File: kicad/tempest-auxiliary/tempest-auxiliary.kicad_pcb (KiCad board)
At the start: 2 copper layers, 188 x 180 mm, 23 parts

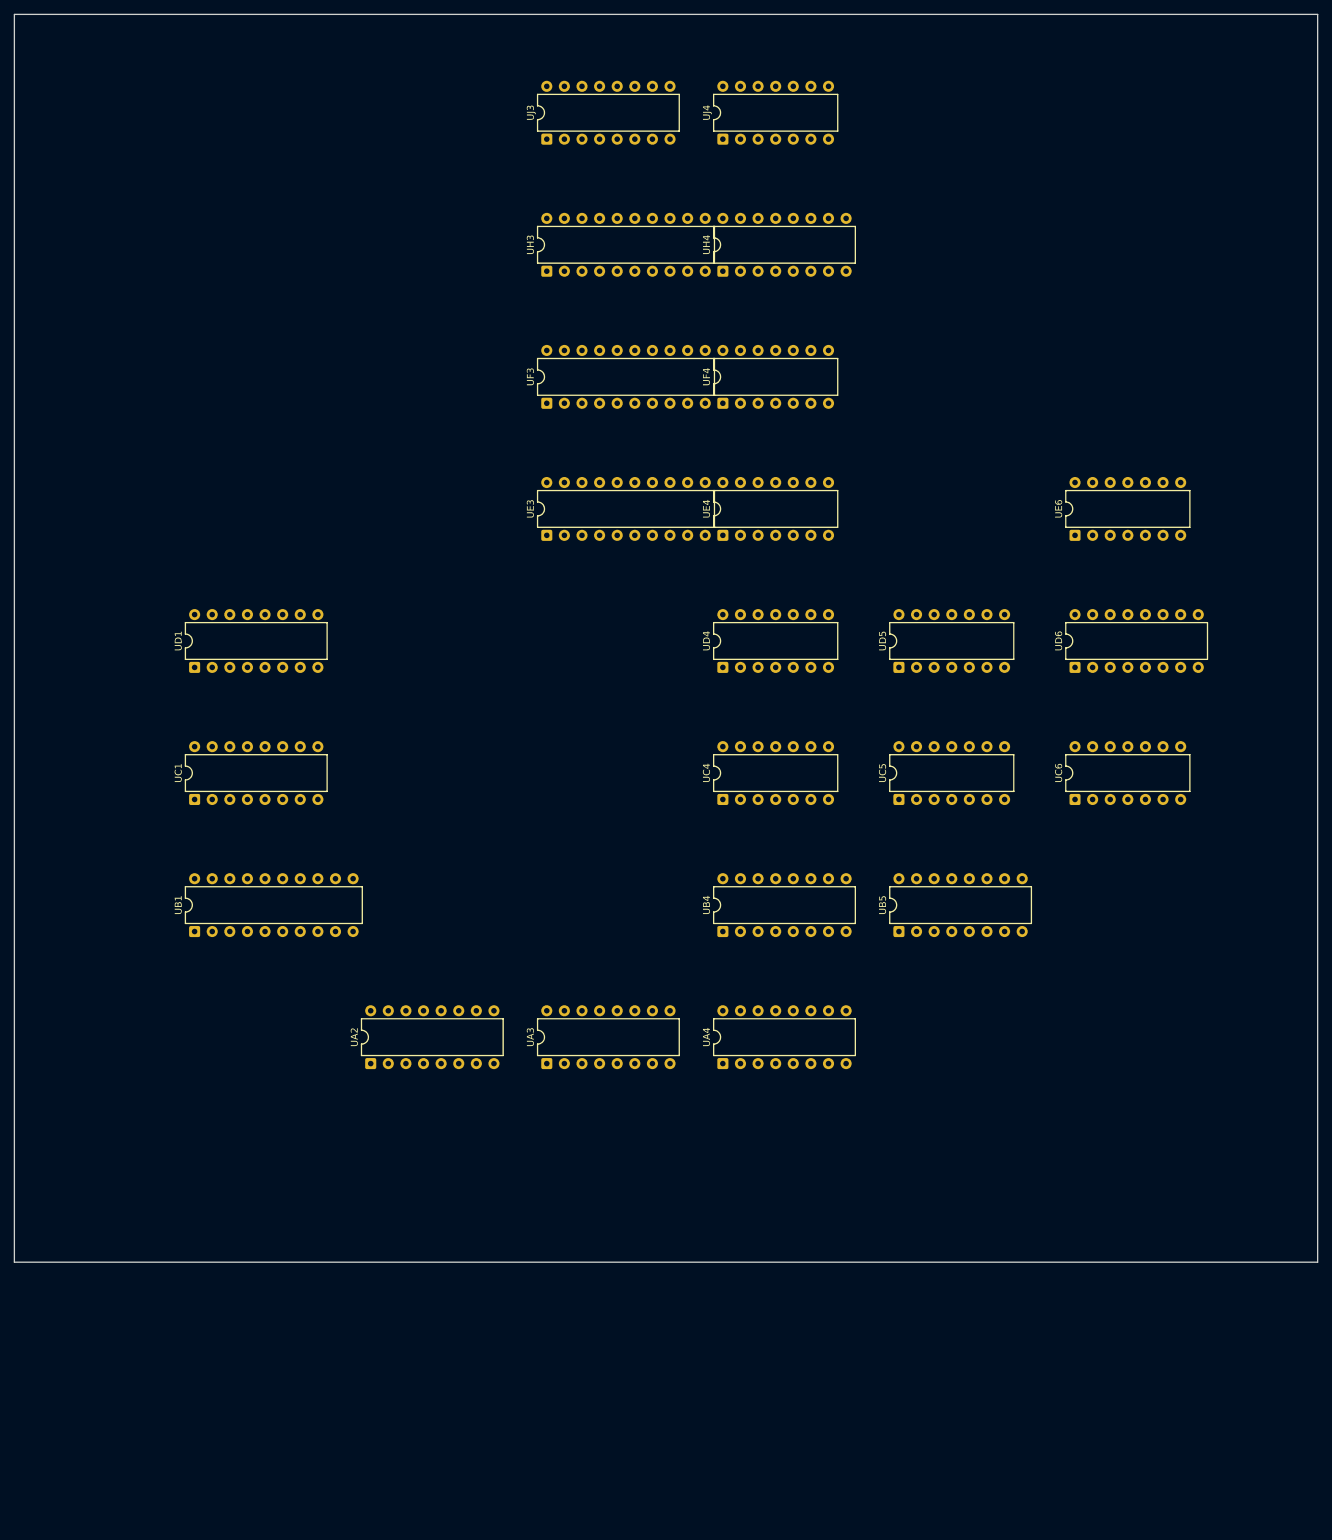
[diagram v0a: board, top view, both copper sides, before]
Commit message: Trace the Tempest Auxiliary PCB in full and redraw it in KiCad
Every connection on DP-190 sheet 3 Side B (Auxiliary PCB 037585-01, 4th
printing, checked against the 2nd and 1st) read into
boards/tempest-auxiliary.nets: 216 nets over 1,036 pins, 41 ICs and 147
passives, connectors and test points. It is not "23 stock parts": the sheet
carries the whole Math Box, the ER2055 high-score EAROM and the charge pump
that makes its -28V, both POKEYs, the spinner inputs and the audio stage.

Checks, all passing:
- build_board_nets.py: 0 problems.
- Every one of the 130 resistor, capacitor and diode values, and all 41 IC
  positions, agree with the TM-190 Figure 22 parts list.
- The Math Box, mapped onto Battlezone's positions, agrees with the
  independently traced Battlezone board on all 79 nets and all 65 signatures.
- check_board_schematic.py: KiCad's netlist of the eleven redrawn sheets
  matches the read, 0 disagreements.

The pipeline is now generic:
- plan_board_schematic.py takes its layout from boards/<slug>.sheets.json
  (Battlezone's plan regenerates byte for byte) and, with --ops, writes every
  label, power symbol and no-connect at an explicit coordinate from the
  symbol geometry -- the way round Konnect's first-unit-only pin queries.
- tools/check_board_sheets.py proves one sheet as soon as it is drawn.
- build_board_nets.py: `parallel` for outputs tied on purpose (K3's four
  LM324 sections), a custom pinout may name a supply pin's rail (the ER2055's
  VSS is +5V), any +/-NV net is a rail, and a net with two sheet names takes
  the first declared rather than whichever hash order picked.
- docs/TRACING-A-BOARD.md is the reader brief and the drawing recipe.

Logged, not guessed: B1 pin 1 is lettered BEGIN but drawn wired to /BEGIN in
all three printings (the read follows the label); K3, R58, C39, three
signatures and R10's supply differ between printings. The site does not
render board notes or conflicts, so the BEGIN one is in the status line too.

ERC has 5 er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
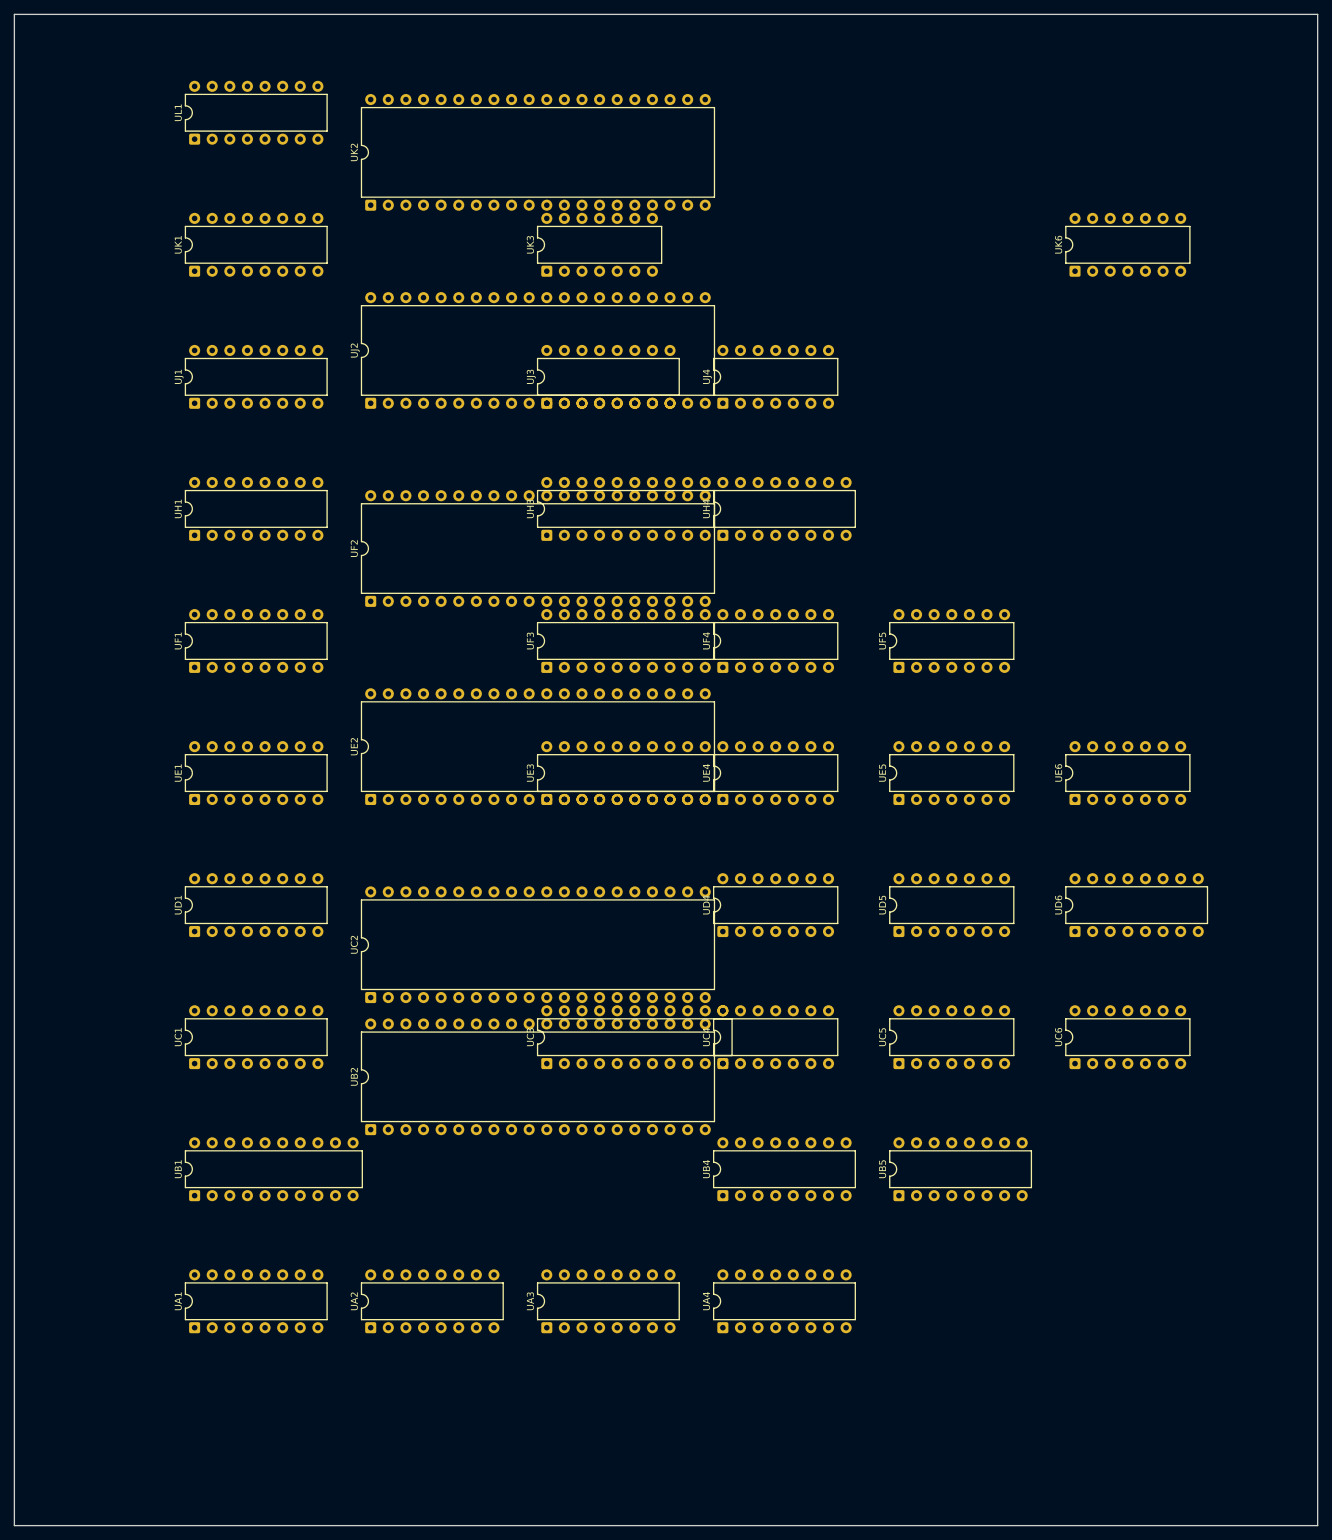
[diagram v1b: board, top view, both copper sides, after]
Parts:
- added UA1: 82S123, DIP-16_W7.62mm, F.Cu at (26.0, 189.4)
- added UB2: C012294-01, DIP-40_W15.24mm, F.Cu at (51.4, 160.9)
- added UC2: C012294-01, DIP-40_W15.24mm, F.Cu at (51.4, 141.8)
- added UC3: ER2055, DIP-22_W7.62mm, F.Cu at (76.8, 151.3)
- added UE1: 82S129, DIP-16_W7.62mm, F.Cu at (26.0, 113.2)
- added UE2: 137004-001, DIP-40_W15.24mm, F.Cu at (51.4, 113.2)
- added UE5: 74S86, DIP-14_W7.62mm, F.Cu at (127.6, 113.2)
- added UF1: 82S129, DIP-16_W7.62mm, F.Cu at (26.0, 94.2)
- added UF2: 137004-001, DIP-40_W15.24mm, F.Cu at (51.4, 84.7)
- added UF5: 74S03, DIP-14_W7.62mm, F.Cu at (127.6, 94.2)
- added UH1: 82S129, DIP-16_W7.62mm, F.Cu at (26.0, 75.2)
- added UJ1: 82S129, DIP-16_W7.62mm, F.Cu at (26.0, 56.1)
- added UJ2: 137004-001, DIP-40_W15.24mm, F.Cu at (51.4, 56.1)
- added UK1: 82S129, DIP-16_W7.62mm, F.Cu at (26.0, 37.0)
- added UK2: 137004-001, DIP-40_W15.24mm, F.Cu at (51.4, 27.5)
- added UK3: LM324, DIP-14_W7.62mm, F.Cu at (76.8, 37.0)
- added UK6: LM324, DIP-14_W7.62mm, F.Cu at (153.0, 37.0)
- added UL1: 82S129, DIP-16_W7.62mm, F.Cu at (26.0, 18.0)
- moved UD1 38.1 mm to (26.0, 132.3)
- moved UD4 38.1 mm to (102.2, 132.3)
- moved UD5 38.1 mm to (127.6, 132.3)
- moved UD6 38.1 mm to (153.0, 132.3)
- moved UH3 38.1 mm to (76.8, 75.2)
- moved UH4 38.1 mm to (102.2, 75.2)
- moved UF3 38.1 mm to (76.8, 94.2)
- moved UF4 38.1 mm to (102.2, 94.2)
- moved UJ3 38.1 mm to (76.8, 56.1)
- moved UJ4 38.1 mm to (102.2, 56.1)
- moved UA2 38.1 mm to (51.4, 189.4)
- moved UA3 38.1 mm to (76.8, 189.4)
- moved UA4 38.1 mm to (102.2, 189.4)
- moved UB1 38.1 mm to (26.0, 170.4)
- moved UB4 38.1 mm to (102.2, 170.4)
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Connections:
- UA2 pad 1: (no net) -> M START
- UA2 pad 16: (no net) -> +5V
- UA2 pad 2: (no net) -> E3MHZ
- UA2 pad 3: (no net) -> /BEGIN
- UA2 pad 4: (no net) -> E6MHZ
- UA2 pad 5: (no net) -> R1-1
- UA2 pad 6: (no net) -> BEGIN
- UA2 pad 7: (no net) -> /BEGIN
- UA2 pad 8: (no net) -> GND
- UA3 pad 1: (no net) -> R1-1
- UA3 pad 10: (no net) -> A3-10
- UA3 pad 11: (no net) -> EAB1
- UA3 pad 12: (no net) -> A3-12
- UA3 pad 13: (no net) -> EAB3
- UA3 pad 14: (no net) -> EAB5
- UA3 pad 15: (no net) -> A3-15
- UA3 pad 16: (no net) -> +5V
- UA3 pad 2: (no net) -> A3-2
- UA3 pad 3: (no net) -> EAB4
- UA3 pad 4: (no net) -> EAB2
- UA3 pad 5: (no net) -> A3-5
- UA3 pad 6: (no net) -> EAB0
- UA3 pad 7: (no net) -> A3-7
- UA3 pad 8: (no net) -> GND
- UA3 pad 9: (no net) -> /EARWR
- UA4 pad 1: (no net) -> GND
- UA4 pad 10: (no net) -> GND
- UA4 pad 11: (no net) -> R54-1
- UA4 pad 14: (no net) -> D6-12
- UA4 pad 15: (no net) -> GND
- UA4 pad 16: (no net) -> +5V
- UA4 pad 2: (no net) -> TBC1
- UA4 pad 3: (no net) -> TBC0
- UA4 pad 4: (no net) -> GND
- UA4 pad 5: (no net) -> C6-5
- UA4 pad 6: (no net) -> TBC2
- UA4 pad 7: (no net) -> TBC3
- UA4 pad 8: (no net) -> GND
- UA4 pad 9: (no net) -> GND
- UB1 pad 1: (no net) -> BEGIN
- UB1 pad 10: (no net) -> GND
- UB1 pad 11: (no net) -> E4-6
- UB1 pad 12: (no net) -> A1-7
- UB1 pad 13: (no net) -> A1
- UB1 pad 14: (no net) -> A3
- UB1 pad 15: (no net) -> A1-5
- UB1 pad 16: (no net) -> A1-3
- UB1 pad 17: (no net) -> A5
- UB1 pad 18: (no net) -> A7
- UB1 pad 19: (no net) -> A1-1
- UB1 pad 2: (no net) -> A1-2
- UB1 pad 20: (no net) -> +5V
- UB1 pad 3: (no net) -> A6
- UB1 pad 4: (no net) -> A4
- UB1 pad 5: (no net) -> A1-4
- UB1 pad 6: (no net) -> A1-6
- UB1 pad 7: (no net) -> A2
- UB1 pad 8: (no net) -> A0
- UB1 pad 9: (no net) -> A1-9
- UB4 pad 1: (no net) -> /I/O
- UB4 pad 11: (no net) -> /EARCON
- UB4 pad 12: (no net) -> /EARWR
- UB4 pad 13: (no net) -> EAB7
- UB4 pad 14: (no net) -> EAB6
- UB4 pad 15: (no net) -> C4-3
- UB4 pad 16: (no net) -> +5V
- UB4 pad 2: (no net) -> EAB6
- UB4 pad 3: (no net) -> EAB7
- UB4 pad 5: (no net) -> B4-5
- UB4 pad 6: (no net) -> B4-6
- UB4 pad 7: (no net) -> B4-7
- UB4 pad 8: (no net) -> GND
- UB5 pad 1: (no net) -> B4-7
- UB5 pad 10: (no net) -> /YLO
- UB5 pad 11: (no net) -> /EARD
- UB5 pad 12: (no net) -> /STREN
- UB5 pad 13: (no net) -> EAB5
- UB5 pad 14: (no net) -> EAB4
- UB5 pad 15: (no net) -> C4-8
- UB5 pad 16: (no net) -> +5V
- UB5 pad 2: (no net) -> EAB4
- UB5 pad 3: (no net) -> EAB5
- UB5 pad 4: (no net) -> /POKEY1
- UB5 pad 5: (no net) -> /POKEY2
- UB5 pad 6: (no net) -> B5-6
- UB5 pad 8: (no net) -> GND
- UB5 pad 9: (no net) -> /YHI
- UC1 pad 1: (no net) -> R1-1
- UC1 pad 10: (no net) -> /PCEN
- UC1 pad 11: (no net) -> SAEN1
- UC1 pad 12: (no net) -> MA6
- UC1 pad 13: (no net) -> MA5
- UC1 pad 14: (no net) -> MA4
- UC1 pad 16: (no net) -> +5V
- UC1 pad 2: (no net) -> CLK
- UC1 pad 3: (no net) -> A1-5
- UC1 pad 4: (no net) -> A1-6
- UC1 pad 5: (no net) -> A1-7
- UC1 pad 6: (no net) -> A1-9
- UC1 pad 7: (no net) -> D1-15
- UC1 pad 8: (no net) -> GND
- UC1 pad 9: (no net) -> /PCEN
- UC4 pad 1: (no net) -> /I/O
- UC4 pad 10: (no net) -> B4-5
- UC4 pad 11: (no net) -> /OL
- UC4 pad 12: (no net) -> B5-6
- UC4 pad 13: (no net) -> /WRITE
- UC4 pad 14: (no net) -> +5V
- UC4 pad 2: (no net) -> /WRITE
- UC4 pad 3: (no net) -> C4-3
- UC4 pad 4: (no net) -> ER/WB
- UC4 pad 5: (no net) -> B4-6
- UC4 pad 6: (no net) -> C4-6
- UC4 pad 7: (no net) -> GND
- UC4 pad 8: (no net) -> C4-8
- UC4 pad 9: (no net) -> R/WB
- UC5 pad 10: (no net) -> R/WB
- UC5 pad 11: (no net) -> EPHI2
- UC5 pad 14: (no net) -> +5V
- UC5 pad 3: (no net) -> F4-6
- UC5 pad 4: (no net) -> EPHI2
- UC5 pad 5: (no net) -> E3MHZ
- UC5 pad 6: (no net) -> SACLK3
- UC5 pad 7: (no net) -> GND
- UC5 pad 8: (no net) -> /WRITE
- UC5 pad 9: (no net) -> E3MHZ
- UC6 pad 1: (no net) -> R54-1
- UC6 pad 14: (no net) -> +5V
- UC6 pad 2: (no net) -> D6-4
- UC6 pad 3: (no net) -> D6-12
- UC6 pad 4: (no net) -> R54-1
- UC6 pad 5: (no net) -> C6-5
- UC6 pad 7: (no net) -> GND
- UD1 pad 1: (no net) -> R1-1
- UD1 pad 10: (no net) -> /PCEN
- UD1 pad 11: (no net) -> MA3
- UD1 pad 12: (no net) -> MA2
- UD1 pad 13: (no net) -> MA1
- UD1 pad 14: (no net) -> MA0
- UD1 pad 15: (no net) -> D1-15
- UD1 pad 16: (no net) -> +5V
- UD1 pad 2: (no net) -> CLK
- UD1 pad 3: (no net) -> A1-1
- UD1 pad 4: (no net) -> A1-2
- UD1 pad 5: (no net) -> A1-3
- UD1 pad 6: (no net) -> A1-4
- UD1 pad 7: (no net) -> R1-1
- UD1 pad 8: (no net) -> GND
- UD1 pad 9: (no net) -> /PCEN
- UD4 pad 1: (no net) -> CLK
- UD4 pad 10: (no net) -> E5-11
- UD4 pad 11: (no net) -> D4-11
- UD4 pad 12: (no net) -> J
- UD4 pad 13: (no net) -> D4-8
- UD4 pad 14: (no net) -> +5V
- UD4 pad 2: (no net) -> BEGIN
- UD4 pad 3: (no net) -> SACLK2
- UD4 pad 4: (no net) -> A18
- UD4 pad 5: (no net) -> A18
- UD4 pad 6: (no net) -> D4-6
- UD4 pad 7: (no net) -> GND
- UD4 pad 8: (no net) -> D4-8
- UD4 pad 9: (no net) -> S
- UD5 pad 1: (no net) -> R54-1
- UD5 pad 10: (no net) -> R54-1
- UD5 pad 11: (no net) -> /CLK
- UD5 pad 12: (no net) -> A12
- UD5 pad 13: (no net) -> /BEGIN
- UD5 pad 14: (no net) -> +5V
- UD5 pad 2: (no net) -> Q0
- UD5 pad 3: (no net) -> CLK
- UD5 pad 4: (no net) -> R54-1
- UD5 pad 6: (no net) -> D5-6
- UD5 pad 7: (no net) -> GND
- UD5 pad 9: (no net) -> STOP
- UD6 pad 1: (no net) -> FLIP
- UD6 pad 10: (no net) -> C52-1
- UD6 pad 11: (no net) -> C53-1
- UD6 pad 12: (no net) -> D6-12
- UD6 pad 13: (no net) -> E6-8
- UD6 pad 14: (no net) -> E6-6
- UD6 pad 15: (no net) -> GND
- UD6 pad 16: (no net) -> +5V
- UD6 pad 2: (no net) -> E6-12
- UD6 pad 3: (no net) -> E6-10
- UD6 pad 4: (no net) -> D6-4
- UD6 pad 5: (no net) -> C50-1
- UD6 pad 6: (no net) -> C51-1
- UD6 pad 7: (no net) -> D6-7
- UD6 pad 8: (no net) -> GND
- UD6 pad 9: (no net) -> D6-9
- UE3 pad 1: (no net) -> /EARD
- UE3 pad 10: (no net) -> GND
- UE3 pad 11: (no net) -> C3-5
- UE3 pad 12: (no net) -> EDB5
- UE3 pad 13: (no net) -> C3-20
- UE3 pad 14: (no net) -> EDB6
- UE3 pad 15: (no net) -> C3-21
- UE3 pad 16: (no net) -> EDB7
- UE3 pad 17: (no net) -> C3-22
- UE3 pad 18: (no net) -> EDB3
- UE3 pad 19: (no net) -> JP1-2
- UE3 pad 2: (no net) -> C3-1
- UE3 pad 20: (no net) -> +5V
- UE3 pad 3: (no net) -> EDB2
- UE3 pad 4: (no net) -> C3-2
- UE3 pad 5: (no net) -> EDB1
- UE3 pad 6: (no net) -> C3-3
- UE3 pad 7: (no net) -> EDB0
- UE3 pad 8: (no net) -> C3-4
- UE3 pad 9: (no net) -> EDB4
- UE4 pad 10: (no net) -> D5-6
- UE4 pad 11: (no net) -> /PCEN
- UE4 pad 12: (no net) -> /BEGIN
- UE4 pad 13: (no net) -> D4-11
- UE4 pad 14: (no net) -> +5V
- UE4 pad 4: (no net) -> /CLK
- UE4 pad 5: (no net) -> LDAB
- UE4 pad 6: (no net) -> E4-6
- UE4 pad 7: (no net) -> GND
- UE4 pad 8: (no net) -> E4-8
- UE4 pad 9: (no net) -> M
- UE6 pad 1: (no net) -> C48-1
- UE6 pad 10: (no net) -> E6-10
- UE6 pad 11: (no net) -> C45-1
- UE6 pad 12: (no net) -> E6-12
- UE6 pad 13: (no net) -> C46-1
- UE6 pad 14: (no net) -> +5V
- UE6 pad 2: (no net) -> E6-2
- UE6 pad 5: (no net) -> C32-1
- UE6 pad 6: (no net) -> E6-6
- UE6 pad 7: (no net) -> GND
- UE6 pad 8: (no net) -> E6-8
- UE6 pad 9: (no net) -> C31-1
- UF3 pad 1: (no net) -> J3-11
- UF3 pad 10: (no net) -> GND
- UF3 pad 11: (no net) -> /EARWR
- UF3 pad 12: (no net) -> C3-5
- UF3 pad 13: (no net) -> H3-12
- UF3 pad 14: (no net) -> H3-14
- UF3 pad 15: (no net) -> C3-20
- UF3 pad 16: (no net) -> C3-21
- UF3 pad 17: (no net) -> H3-16
- UF3 pad 18: (no net) -> H3-18
- UF3 pad 19: (no net) -> C3-22
- UF3 pad 2: (no net) -> C3-1
- UF3 pad 20: (no net) -> +5V
- UF3 pad 3: (no net) -> H3-3
- UF3 pad 4: (no net) -> H3-5
- UF3 pad 5: (no net) -> C3-2
- UF3 pad 6: (no net) -> C3-3
- UF3 pad 7: (no net) -> EDB6
- UF3 pad 8: (no net) -> H3-9
- UF3 pad 9: (no net) -> C3-4
- UF4 pad 1: (no net) -> CLK
- UF4 pad 10: (no net) -> R/WB
- UF4 pad 11: (no net) -> ER/WB
- UF4 pad 12: (no net) -> F4-12
- UF4 pad 13: (no net) -> /STREN
- UF4 pad 14: (no net) -> +5V
- UF4 pad 2: (no net) -> /CLK
- UF4 pad 5: (no net) -> C4-6
- UF4 pad 6: (no net) -> F4-6
- UF4 pad 7: (no net) -> GND
- UF4 pad 8: (no net) -> F4-8
- UF4 pad 9: (no net) -> /EARD
- UH3 pad 1: (no net) -> GND
- UH3 pad 10: (no net) -> GND
- UH3 pad 11: (no net) -> EDB5
- UH3 pad 12: (no net) -> H3-12
- UH3 pad 13: (no net) -> E3MHZ-IN
- UH3 pad 14: (no net) -> H3-14
- UH3 pad 15: (no net) -> EDB7
- UH3 pad 16: (no net) -> H3-16
- UH3 pad 17: (no net) -> EDB3
- UH3 pad 18: (no net) -> H3-18
- UH3 pad 19: (no net) -> JP3-2
- UH3 pad 2: (no net) -> EDB2
- UH3 pad 20: (no net) -> +5V
- UH3 pad 3: (no net) -> H3-3
- UH3 pad 4: (no net) -> EDB1
- UH3 pad 5: (no net) -> H3-5
- UH3 pad 6: (no net) -> EDB0
- UH3 pad 7: (no net) -> E3MHZ
- UH3 pad 8: (no net) -> EDB4
- UH3 pad 9: (no net) -> H3-9
- UH4 pad 1: (no net) -> /RESET
- UH4 pad 10: (no net) -> FLIP
- UH4 pad 11: (no net) -> EDB2
- UH4 pad 12: (no net) -> H4-12
- UH4 pad 13: (no net) -> EDB1
- UH4 pad 14: (no net) -> EDB0
- UH4 pad 15: (no net) -> H4-15
- UH4 pad 16: (no net) -> +5V
- UH4 pad 6: (no net) -> EDB3
- UH4 pad 7: (no net) -> SAEN 2,3
- UH4 pad 8: (no net) -> GND
- UH4 pad 9: (no net) -> /OL
- UJ3 pad 1: (no net) -> /RESET
- UJ3 pad 11: (no net) -> J3-11
- UJ3 pad 12: (no net) -> H3-18
- UJ3 pad 13: (no net) -> H3-16
- UJ3 pad 15: (no net) -> J3-15
- UJ3 pad 16: (no net) -> +5V
- UJ3 pad 2: (no net) -> J3-2
- UJ3 pad 4: (no net) -> H3-3
- UJ3 pad 5: (no net) -> H3-14
- UJ3 pad 7: (no net) -> J3-7
- UJ3 pad 8: (no net) -> GND
- UJ3 pad 9: (no net) -> /EARCON
- UJ4 pad 1: (no net) -> CLK
- UJ4 pad 14: (no net) -> +5V
- UJ4 pad 2: (no net) -> E3MHZ
- UJ4 pad 3: (no net) -> STOP
- UJ4 pad 4: (no net) -> M START
- UJ4 pad 5: (no net) -> C4-6
- UJ4 pad 6: (no net) -> EPHI2
- UJ4 pad 7: (no net) -> GND
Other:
- board size 188 x 180 mm -> 188 x 218 mm
